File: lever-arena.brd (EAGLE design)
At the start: 77 x 56 mm, 24 parts, among them J1 POWER_JACKPTH_BREAD

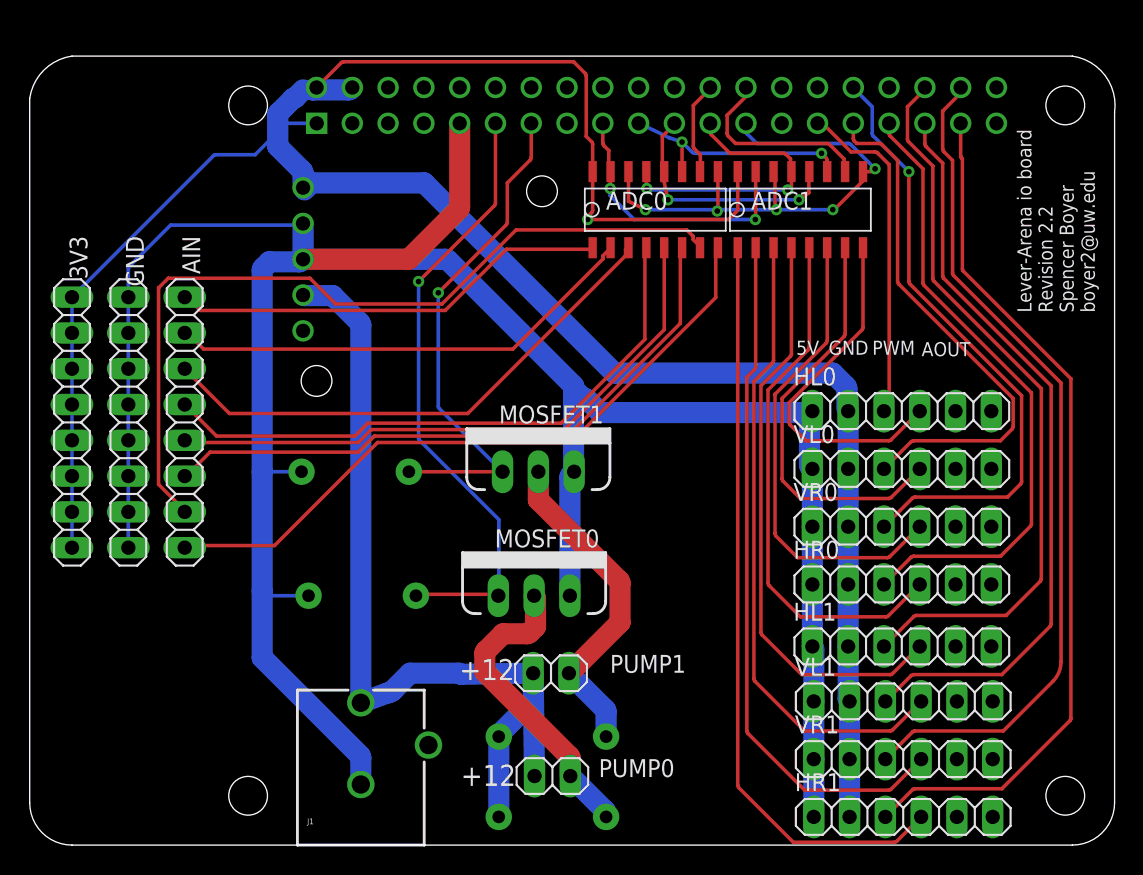
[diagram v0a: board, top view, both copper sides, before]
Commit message: added labels
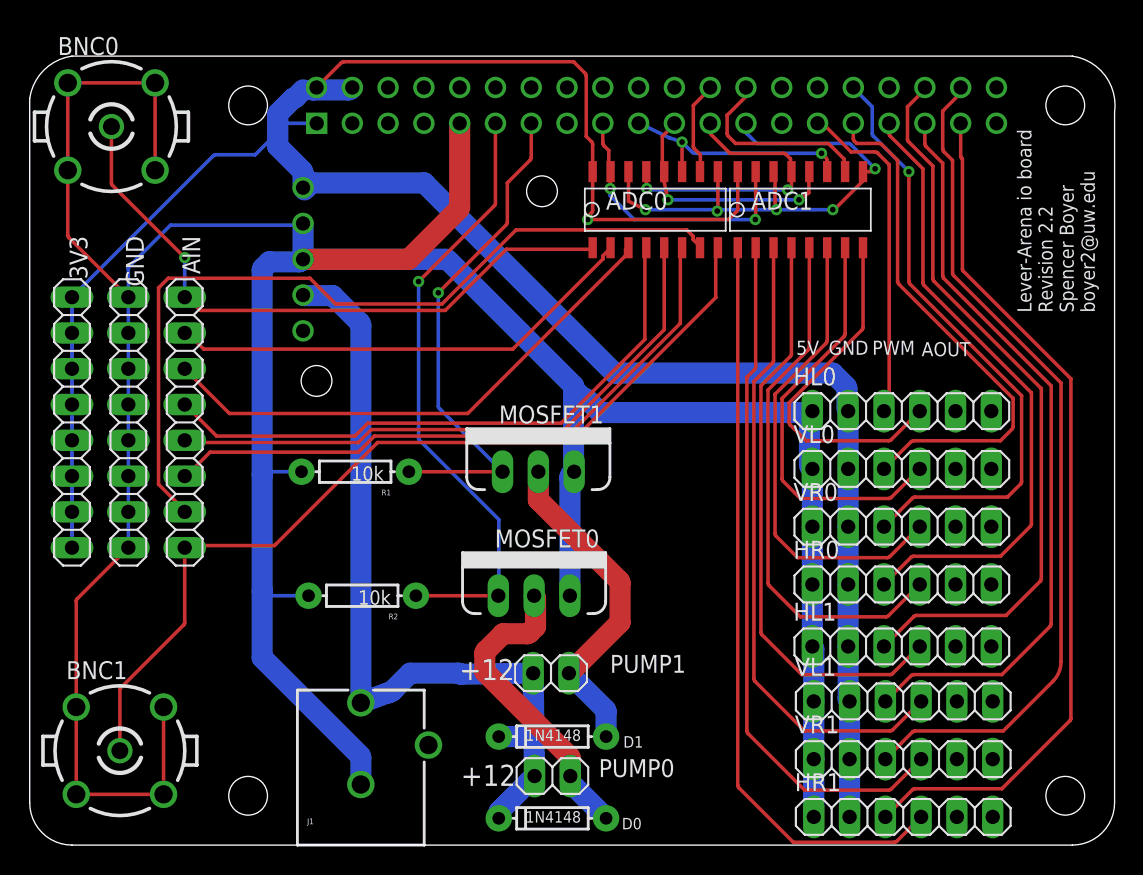
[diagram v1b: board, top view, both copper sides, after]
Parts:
- removed D2: 1N4148, SparkFun-DiscreteSemi:DIODE-1N4148
- added BNC0, BNC1: BN35N61, con-coax:B35N61
- added D0: 1N4148, SparkFun-DiscreteSemi:DIODE-1N4148
- moved D1 5.70 mm to (37.1, 7.70), flipped to the top, turned to 180 degrees
- flipped R1 to the top, turned to 180 degrees
- flipped R2 to the top, turned to 180 degrees
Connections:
- removed net N$1: ADC0.CH0, AIN.1
- removed net N$17: ADC0.CH7, AIN.8
- new net N$3: ADC0.CH0, AIN.1, BNC0.1
- new net N$6: ADC0.CH7, AIN.8, BNC1.1
- net 12V: now also D0.C, D1.A; no longer D2.A, D2.C
- net GND: now also BNC0.2, BNC0.3, BNC0.4, BNC0.5, BNC1.2, BNC1.3, BNC1.4, BNC1.5
- net N$4: now also D0.A; no longer D1.A
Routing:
- net N$6: track 0.00 -> 65.0 mm
- net GND: track 225.9 -> 286.7 mm
- net N$17: track 48.6 -> 0.00 mm
- net N$3: track 0.00 -> 45.4 mm, vias 0 -> 1
- net N$1: track 31.2 -> 0.00 mm
- net 12V: track 85.1 -> 82.4 mm

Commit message: Revision 2.3
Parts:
- REGULATOR: device spencer:POLOLU5V -> spencer:POLOLU5VI
- moved BNC1 6.87 mm to (8.30, 13.3)
- flipped REGULATOR to the top, turned to 270 degrees
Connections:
- new net N$1: BNC0.1, PCB1.P$3
- new net N$5: BNC1.1, PCB1.P$5
- net N$3: no longer BNC0.1
- net N$6: no longer BNC1.1
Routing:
- net N$5: track 0.00 -> 50.4 mm, vias 0 -> 1
- net N$1: track 0.00 -> 19.5 mm
- net N$6: track 65.0 -> 48.6 mm
- net N$3: track 45.4 -> 31.2 mm, vias 1 -> 0
- net GND: track 286.7 -> 272.6 mm
- net 12V: track 82.4 -> 82.9 mm
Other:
- board text added: "Lever-Arena io board Revision 2.3 Spencer Boyer boyer2@uw.edu"
- board text removed: "Lever-Arena io board Revision 2.2 Spencer Boyer boyer2@uw.edu"

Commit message: 2.3
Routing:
- net GND: track 272.6 -> 280.1 mm
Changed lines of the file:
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@@
 <layer number="25" name="tNames" color="7" fill="1" visible="yes" active="yes"/>
 <layer number="26" name="bNames" color="7" fill="1" visible="yes" active="yes"/>
-<layer number="27" name="tValues" color="7" fill="1" visible="no" active="yes"/>
+<layer number="27" name="tValues" color="7" fill="1" visible="yes" active="yes"/>
 <layer number="28" name="bValues" color="7" fill="1" visible="yes" active="yes"/>
 <layer number="29" name="tStop" color="7" fill="3" visible="no" active="yes"/>
@@
 <layer number="42" name="bRestrict" color="1" fill="10" visible="yes" active="yes"/>
 <layer number="43" name="vRestrict" color="2" fill="10" visible="yes" active="yes"/>
-<layer number="44" name="Drills" color="7" fill="1" visible="no" active="yes"/>
-<layer number="45" name="Holes" color="7" fill="1" visible="no" active="yes"/>
+<layer number="44" name="Drills" color="7" fill="1" visible="yes" active="yes"/>
+<layer number="45" name="Holes" color="7" fill="1" visible="yes" active="yes"/>
 <layer number="46" name="Milling" color="3" fill="1" visible="no" active="yes"/>
 <layer number="47" name="Measures" color="7" fill="1" visible="no" active="yes"/>
@@
 <layer number="49" name="Reference" color="7" fill="1" visible="yes" active="yes"/>
 <layer number="50" name="dxf" color="7" fill="1" visible="no" active="no"/>
-<layer number="51" name="tDocu" color="7" fill="1" visible="no" active="yes"/>
+<layer number="51" name="tDocu" color="7" fill="1" visible="yes" active="yes"/>
 <layer number="52" name="bDocu" color="7" fill="1" visible="yes" active="yes"/>
 <layer number="53" name="tGND_GNDA" color="7" fill="9" visible="no" active="no"/>
@@
 Spencer Boyer
 boyer2@uw.edu</text>
-<text x="13.1" y="20.9" size="1" layer="22" rot="MR90">7    6    5    4    3    2    1    0</text>
+<text x="14" y="21" size="1" layer="21" rot="R90">7    6    5    4    3    2    1    0</text>
 </plain>
 <attributes>
@@
 <wire x1="19.5" y1="46.9" x2="19.32560625" y2="46.9" width="1.5" layer="16"/>
 <wire x1="19.32560625" y1="46.9" x2="19.32560625" y2="47.87439375" width="1.5" layer="16"/>
+<wire x1="19.5" y1="46.9" x2="20.105209375" y2="46.9" width="1.5" layer="16"/>
+<wire x1="20.105209375" y1="46.9" x2="20.105209375" y2="47" width="1.5" layer="16"/>
 <wire x1="19.4" y1="53.6" x2="20.079590625" y2="53.6" width="0" layer="19" extent="16-16"/>
 <wire x1="58.09" y1="30.8" x2="58" y2="31" width="0" layer="19" extent="16-16"/>
-<wire x1="19.5" y1="46.9" x2="20.105209375" y2="46.9" width="1.5" layer="16"/>
-<wire x1="20.105209375" y1="46.9" x2="20.105209375" y2="47" width="1.5" layer="16"/>
 </signal>
 <signal name="GND">
@@
 <wire x1="11.3988" y1="16.3988" x2="5.2012" y2="16.3988" width="0.254" layer="16"/>
 <wire x1="11.3988" y1="10.2012" x2="5.2012" y2="10.2012" width="0.254" layer="16"/>
+<wire x1="26.9" y1="41.58" x2="19.4" y2="41.58" width="1.5" layer="1"/>
 <wire x1="30.5166" y1="45.301809375" x2="42.5" y2="45.7" width="0" layer="19" extent="1-1"/>
-<wire x1="29.514790625" y1="41.58" x2="26.9" y2="41.58" width="0" layer="19" extent="1-16"/>
 </signal>
 <signal name="3V3">
@@
 <wire x1="33.29" y1="7.7" x2="35.791365625" y2="7.7" width="1.5" layer="16"/>
 <wire x1="35.791365625" y1="7.7" x2="35.79164375" y2="7.699884375" width="1.5" layer="16" curve="-45"/>
-<wire x1="35.73" y1="12.2" x2="38.27" y2="12.2" width="0" layer="19" extent="1-1"/>
 <wire x1="33.29" y1="1.9" x2="33.29" y2="2.27715625" width="1.5" layer="16"/>
 <wire x1="33.29" y1="2.27715625" x2="33.348578125" y2="2.418578125" width="1.5" layer="16" curve="-45"/>
@@
 <wire x1="20" y1="39" x2="19.4" y2="39" width="0.254" layer="16"/>
 <wire x1="19.4" y1="39" x2="19.4" y2="39.04" width="0.254" layer="16"/>
+<wire x1="35.73" y1="12.2" x2="38.27" y2="12.2" width="0" layer="19" extent="1-1"/>
 </signal>
 <signal name="N$2">

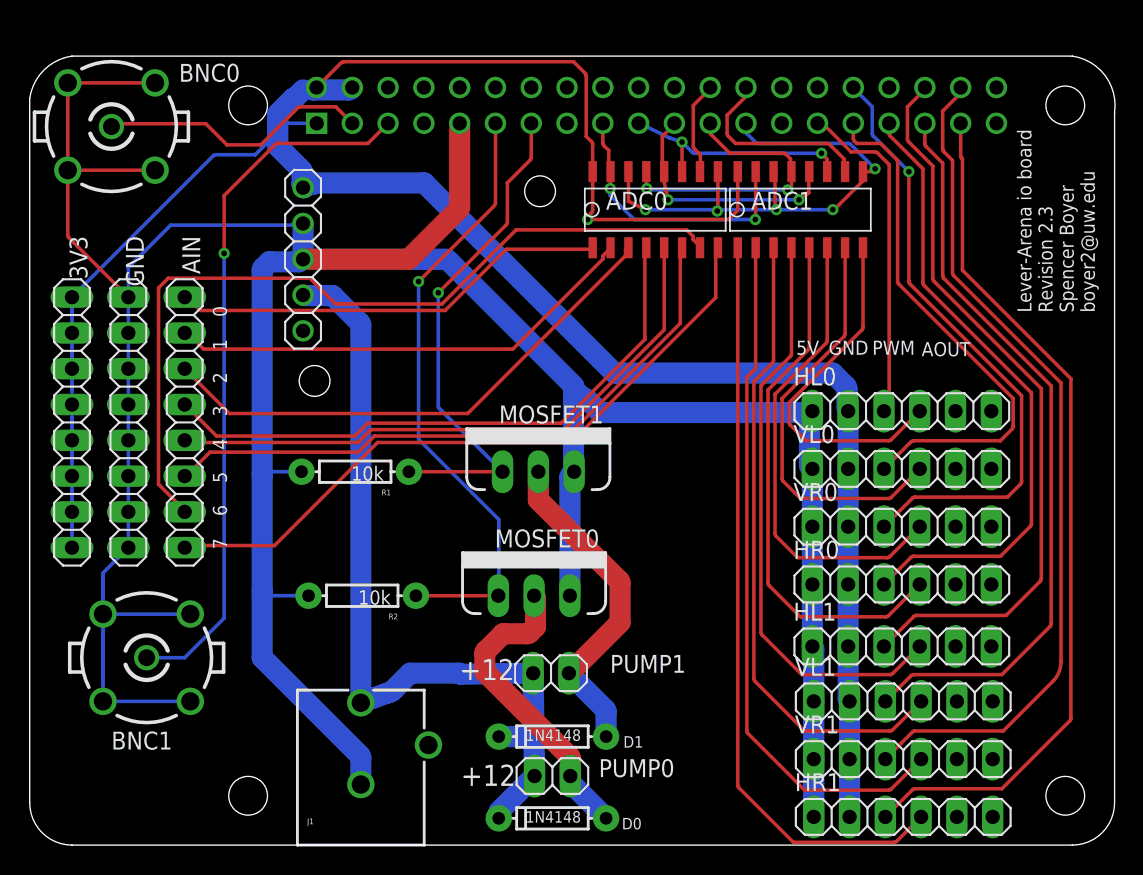
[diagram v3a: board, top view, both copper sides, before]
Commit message: Revision 2.4
routed connectors for adc input
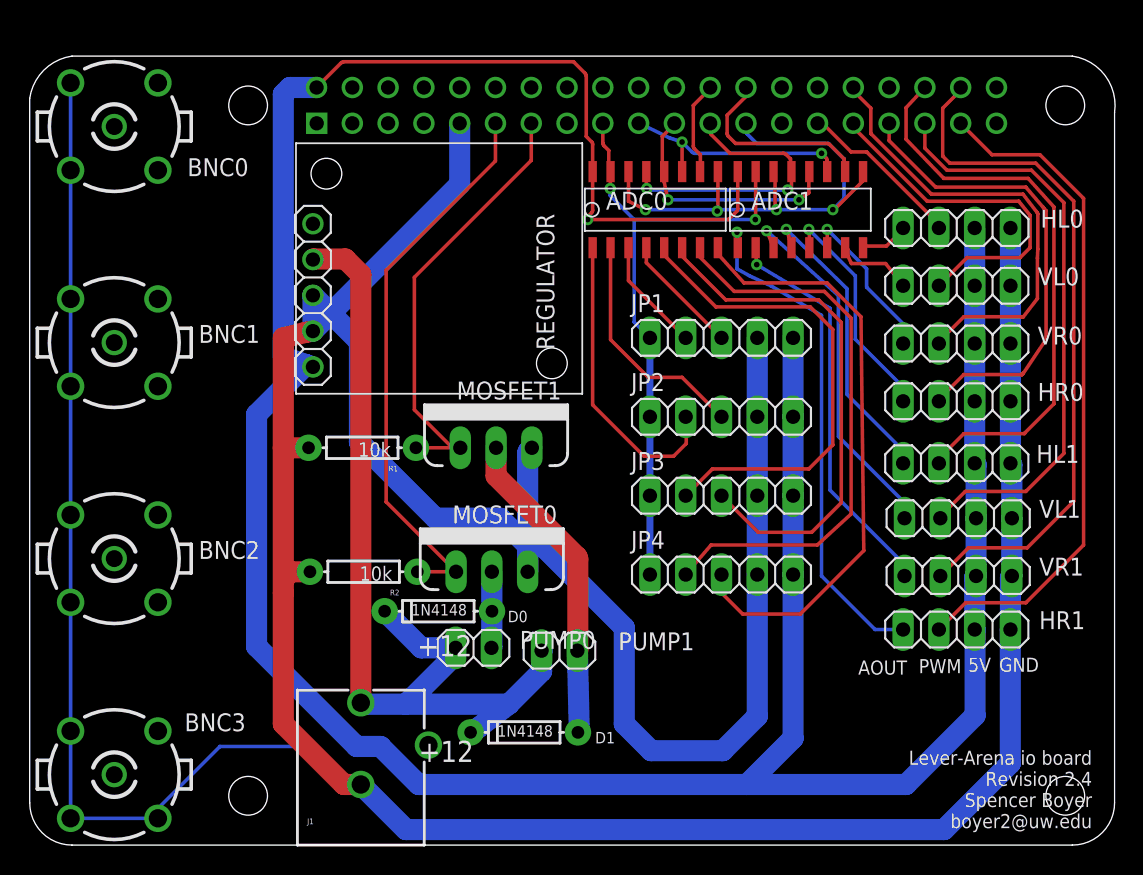
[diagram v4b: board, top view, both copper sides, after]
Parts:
- removed 3V3: 3v3, pinhead:1X08
- removed AIN: AIN, pinhead:1X08
- removed GND: GND, pinhead:1X08
- added BNC2, BNC3: BN35N61, con-coax:B35N61
- added JP1, JP2, JP3, JP4: (no value), pinhead:1X05
- HL0, HL1, HR0, HR1, VL0, VL1, VR0, VR1: device pinhead:1X06 -> pinhead:1X04
- REGULATOR: device spencer:POLOLU5VI -> spencer:POLOLU5V
- moved BNC1 22.5 mm to (6.00, 35.7)
- moved D0 16.8 mm to (29.0, 16.6)
- moved HR1 13.8 mm to (65.8, 15.3)
- moved VR1 13.6 mm to (65.9, 19.1)
- moved VL0 13.6 mm to (65.8, 39.7)
- moved VL1 13.6 mm to (65.9, 23.2)
- moved HL1 13.6 mm to (65.8, 27.1)
- moved HR0 13.6 mm to (65.8, 31.5)
- moved VR0 13.6 mm to (65.8, 35.6)
- moved HL0 13.6 mm to (65.8, 43.8)
- moved PUMP0 10.7 mm to (31.5, 14.0)
- moved REGULATOR 7.63 mm to (20.1, 44.1)
- moved MOSFET0 3.45 mm to (32.8, 19.4)
- moved MOSFET1 3.45 mm to (33.1, 28.2)
- moved D1 2.02 mm to (35.1, 8.00)
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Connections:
- removed net N$11: ADC0.CH1, AIN.2
- removed net N$22: ADC1.CH7, HL0.4
- removed net N$23: ADC1.CH6, VL0.4
- removed net N$27: ADC1.CH5, VR0.4
- removed net N$29: ADC1.CH0, HR1.4
- removed net N$31: ADC1.CH1, VR1.4
- removed net N$6: ADC0.CH7, AIN.8
- new net N$17: ADC0.CH0, JP2.2
- new net N$20: ADC1.CH5, VR0.1
- new net N$34: ADC0.CH4, JP3.2
- new net N$36: ADC1.CH1, VR1.1
- new net N$39: ADC0.CH7, JP4.3
- new net N$40: ADC0.CH6, JP4.2
- new net N$7: PCB1.P$5
- new net N$8: PCB1.P$3
- new net NGNG: ADC1.CH4, HR0.1
- net 3V3: now also JP1.1, JP2.1, JP3.1, JP4.1; no longer 3V3.1, 3V3.2, 3V3.3, 3V3.4, 3V3.5, 3V3.6, 3V3.7, 3V3.8
- net 5V: now also HL0.3, HL1.3, HR0.3, HR1.3, JP1.5, JP2.5, JP3.5, JP4.5, VL0.3, VL1.3, VR0.3, VR1.3; no longer HL0.2, HL1.2, HR0.2, HR1.2, VL0.2, VL1.2, VR0.2, VR1.2
- net GND: now also BNC2.2, BNC2.3, BNC2.4, BNC2.5, BNC3.2, BNC3.3, BNC3.4, BNC3.5, HL0.4, HL1.4, HR0.4, HR1.4, JP1.4, JP2.4, JP3.4, JP4.4, VL0.4, VL1.4, VR0.4, VR1.4; no longer GND.1, GND.2, GND.3, GND.4, GND.5, GND.6, GND.7, GND.8, HL0.1, HL1.1, HR0.1, HR1.1, VL0.1, VL1.1, VR0.1, VR1.1
- net HL0: now also HL0.2; no longer HL0.3
- net HL1: now also HL1.2; no longer HL1.3
- net HR0: now also HR0.2; no longer HR0.3
- net HR1: now also HR1.2; no longer HR1.3
- net N$1: now also PCB1.P$8; no longer BNC0.1, PCB1.P$3
- net N$12: now also ADC1.CH7, HL0.1; no longer ADC0.CH2, AIN.3
- net N$13: now also JP1.3; no longer AIN.4
- net N$14: now also ADC0.CH2, JP1.2; no longer ADC0.CH4, AIN.5
- net N$15: now also ADC0.CH1, JP2.3; no longer ADC0.CH5, AIN.6
- net N$16: now also ADC1.CH6, VL0.1; no longer ADC0.CH6, AIN.7
- net N$28: now also ADC1.CH3, HL1.1; no longer ADC1.CH4, HR0.4
- net N$3: now also ADC1.CH0, HR1.1; no longer ADC0.CH0, AIN.1
- net N$32: now also VL1.1; no longer VL1.4
- net N$33: now also ADC0.CH5, JP3.3; no longer ADC1.CH3, HL1.4
- net N$5: now also PCB1.P$7; no longer BNC1.1, PCB1.P$5
- net VL0: now also VL0.2; no longer VL0.3
- net VL1: now also VL1.2; no longer VL1.3
- net VR0: now also VR0.2; no longer VR0.3
- net VR1: now also VR1.2; no longer VR1.3
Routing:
- net 5V: track 131.6 -> 214.5 mm
- net GND: track 280.1 -> 358.3 mm, vias 5 -> 4
- net N$29: track 53.6 -> 0.00 mm
- net N$16: track 59.0 -> 5.72 mm
- net N$5: track 50.4 -> 0.00 mm, vias 1 -> 0
- net N$31: track 49.6 -> 0.00 mm
- net N$6: track 48.6 -> 0.00 mm
- net N$39: track 0.00 -> 43.0 mm
- net N$40: track 0.00 -> 40.7 mm
- net N$14: track 43.2 -> 8.08 mm
- net N$34: track 0.00 -> 34.8 mm
- net N$12: track 37.9 -> 3.49 mm
- net N$13: track 43.0 -> 8.61 mm
- net N$11: track 33.8 -> 0.00 mm
- net N$27: track 33.7 -> 0.00 mm
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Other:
- board text added: "Lever-Arena io board Revision 2.4 Spencer Boyer boyer2@uw.edu"
- board text removed: "7 6 5 4 3 2 1 0"
- board text removed: "Lever-Arena io board Revision 2.3 Spencer Boyer boyer2@uw.edu"

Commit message: REVISION 2.5
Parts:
- added U$1, U$2, U$3, U$4: SPDTSWITCH, spencer:JS202011CQNSPDT
- LL0: value (none) -> LL0
- LL1: value (none) -> LL1
- RL0: value (none) -> RL0
- RL1: value (none) -> RL1
- moved D0 1.70 mm to (30.7, 16.6)
- moved R1 1.10 mm to (24.7, 28.2)
- moved R2 0.70 mm to (24.4, 19.4)
- renumbered JP1 to LL0, JP2 to RL0, JP3 to LL1, JP4 to RL1
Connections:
- new net N$10: BNC2.1, U$3.P$1, U$3.P$5
- new net N$11: BNC3.1, U$4.P$1, U$4.P$5
- new net N$6: BNC0.1, U$1.P$1, U$1.P$5
- new net N$9: BNC1.1, U$2.P$1, U$2.P$5
- net N$1: now also U$3.P$3, U$3.P$6
- net N$33: now also U$2.P$2, U$2.P$4
- net N$34: now also U$1.P$2, U$1.P$4
- net N$39: now also U$4.P$2, U$4.P$4
- net N$40: now also U$3.P$2, U$3.P$4
- net N$5: now also U$4.P$3, U$4.P$6
- net N$7: now also U$2.P$3, U$2.P$6
- net N$8: now also U$1.P$3, U$1.P$6
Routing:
- net N$34: track 34.8 -> 130.2 mm, vias 0 -> 1
- net N$33: track 37.1 -> 122.8 mm, vias 0 -> 1
- net N$40: track 40.7 -> 120.7 mm, vias 0 -> 1
- net N$39: track 43.0 -> 107.6 mm
- net N$5: track 0.00 -> 55.8 mm, vias 0 -> 2
- net GND: track 358.3 -> 401.6 mm, vias 4 -> 3
- net N$1: track 0.00 -> 39.8 mm
- net N$7: track 0.00 -> 24.2 mm
- net N$8: track 0.00 -> 18.1 mm
- net N$11: track 0.00 -> 13.7 mm
- net N$10: track 0.00 -> 13.5 mm
- net N$6: track 0.00 -> 10.6 mm
- net N$9: track 0.00 -> 9.56 mm
- net N$4: track 5.41 -> 7.79 mm
- net PUMP2: track 30.7 -> 29.6 mm
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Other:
- board text added: "3v"
- board text added: "AIN"
- board text added: "DOUT"
- board text added: "Lever-Arena io board Revision 2.5 Spencer Boyer boyer2@uw.edu"
- board text removed: "AOUT"
- board text removed: "Lever-Arena io board Revision 2.4 Spencer Boyer boyer2@uw.edu"
